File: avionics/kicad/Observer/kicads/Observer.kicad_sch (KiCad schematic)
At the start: 66 parts, among them Q1 AO3400 logic-level N-MOSFET, T1 Wurth 749010012A, T1_CMC1 SRF2012-100Y, T1_CMC2 SRF2012-100Y, T1_D1 PRTR5V0U2X, T1_D2 PRTR5V0U2X, T2 Wurth 749010012A, T2_CMC1 SRF2012-100Y, T2_CMC2 SRF2012-100Y, T2_D1 PRTR5V0U2X, T2_D2 PRTR5V0U2X, U2 Microchip KSZ9477, U3 TI MSPM0G3519-Q1, U4 TI ISOW1044BDFMR, U5 Infineon SLB 9672AU2.0, U6 TI ISOW1412, Y1 25MHz

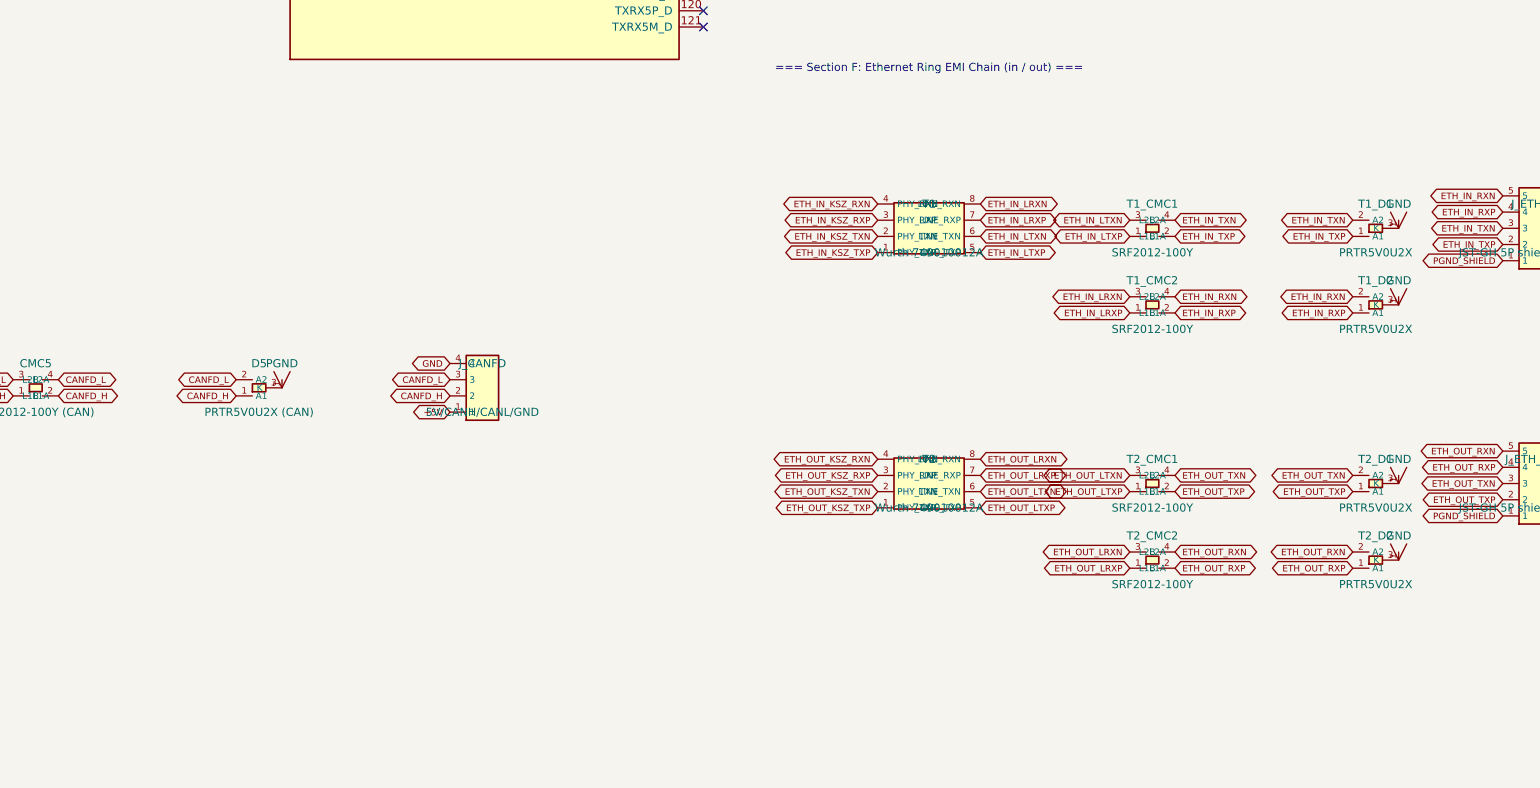
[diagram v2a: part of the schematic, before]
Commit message: fix(avionics): PRTR5V0U2X package/pinout fix on all 12 instances, 5 boards
Owner-approved 2026-09-26 (avionics/WBS.md U7.2). Per Nexperia
PRTR5V0U2X datasheet Table 2 (SOT143B: 1=GND, 2=I/O1, 3=I/O2, 4=VCC),
relinked via tools/kicad_relink.py --rewire (same footprint position/
rotation preserved, only package + pin-to-net correspondence corrected):

- Pilot TVS-CAN, TVS-RS485; TACCO TVS-CAN, TVS-RS485; FlightEngineer
  D_I2C: straightforward SOT-363->SOT-143 swap with existing GND/VCC
  nets carried over unchanged (5 instances).
- Observer T1_D1/T1_D2/T2_D1/T2_D2 (Ethernet magnetics ESD) and D5
  (CAN-FD), Commo 'ANT TVS' and 'UART TVS': these had no VCC net at
  all in the original (wrong-package) design -- VCC tied to the local
  GND/PGND net as a conservative fallback (line-to-line and
  line-to-ground clamping preserved; the rail-clamp direction is
  inert). This is a judgment call, not a datasheet requirement --
  flagged for review, not a silent assumption (7 instances).

ERC unchanged (0/0/0/0/154-pre-existing) on all 5 boards; DRC/parity
flat or improved except one new courtyard-overlap warning on Pilot
(TVS-CAN vs C-IN1, mechanical only) left unresolved rather than guess
a nudge direction without full layout context.

AI-authored: Claude Sonnet 5 (Anthropic).

Co-Authored-By: Claude Sonnet 5 <noreply@anthropic.com>
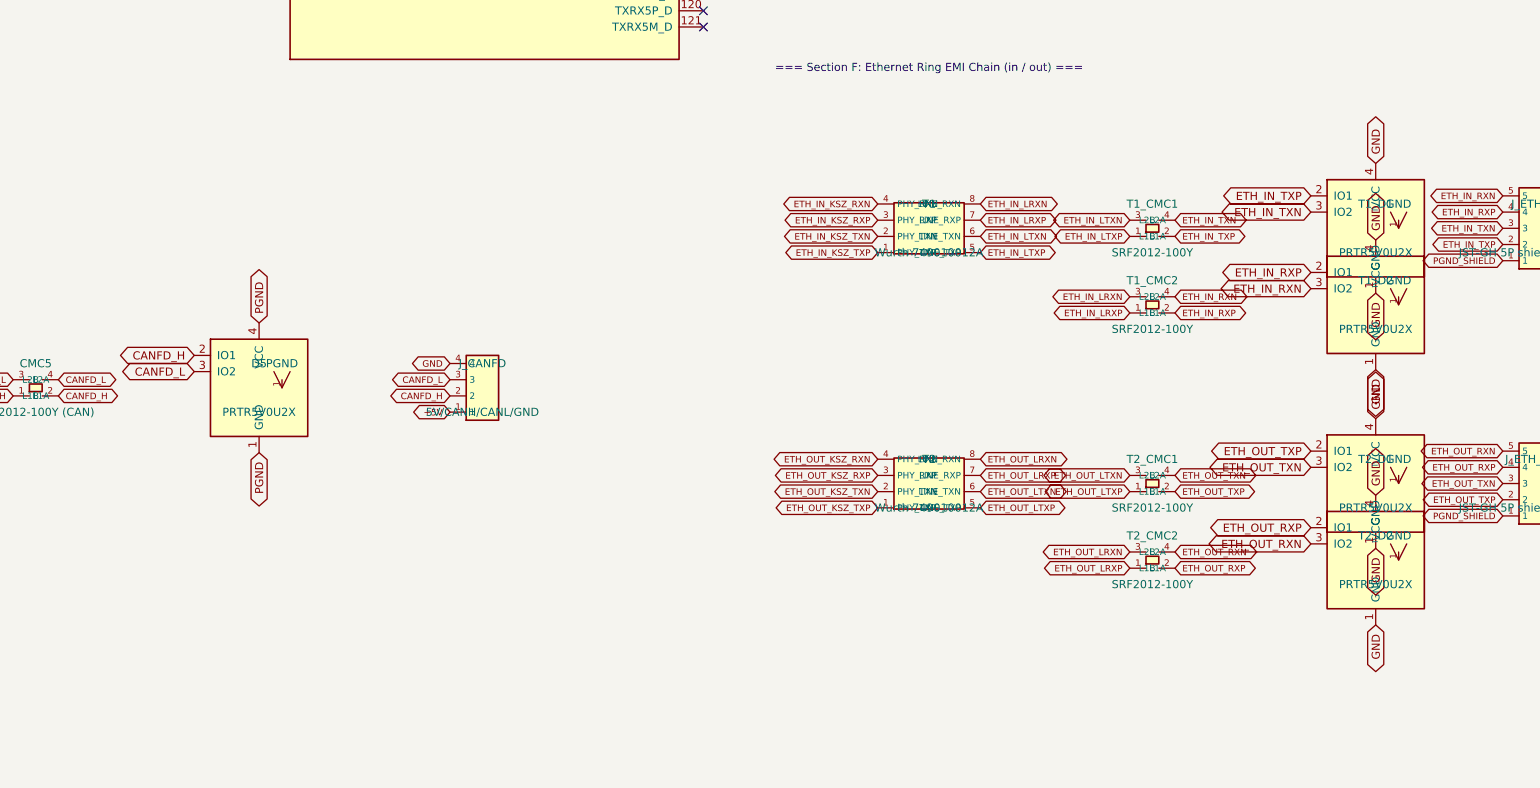
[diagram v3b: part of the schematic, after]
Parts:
- D5: value PRTR5V0U2X (CAN) -> PRTR5V0U2X; footprint Package_TO_SOT_SMD:SOT-363_SC-70-6 -> Package_TO_SOT_SMD:SOT-143; symbol NEXPERIA_PRTR5V0U2X -> SecureControllers:PRTR5V0U2X
- T1_D1, T1_D2, T2_D1, T2_D2: footprint Package_TO_SOT_SMD:SOT-363_SC-70-6 -> Package_TO_SOT_SMD:SOT-143; symbol NEXPERIA_PRTR5V0U2X -> SecureControllers:PRTR5V0U2X
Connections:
- net CANFD_H: now also D5.2 (IO1); no longer D5.1 (A1)
- net CANFD_L: now also D5.3 (IO2); no longer D5.2 (A2)
- net ETH_IN_RXN: now also T1_D2.3 (IO2); no longer T1_D2.2 (A2)
- net ETH_IN_RXP: now also T1_D2.2 (IO1); no longer T1_D2.1 (A1)
- net ETH_IN_TXN: now also T1_D1.3 (IO2); no longer T1_D1.2 (A2)
- net ETH_IN_TXP: now also T1_D1.2 (IO1); no longer T1_D1.1 (A1)
- net ETH_OUT_RXN: now also T2_D2.3 (IO2); no longer T2_D2.2 (A2)
- net ETH_OUT_RXP: now also T2_D2.2 (IO1); no longer T2_D2.1 (A1)
- net ETH_OUT_TXN: now also T2_D1.3 (IO2); no longer T2_D1.2 (A2)
- net ETH_OUT_TXP: now also T2_D1.2 (IO1); no longer T2_D1.1 (A1)
- net GND: now also T1_D1.1 (GND), T1_D1.4 (VCC), T1_D2.1 (GND), T1_D2.4 (VCC), T2_D1.1 (GND), T2_D1.4 (VCC), T2_D2.1 (GND), T2_D2.4 (VCC); no longer T1_D1.3 (K), T1_D2.3 (K), T2_D1.3 (K), T2_D2.3 (K)
- net PGND: now also D5.1 (GND), D5.4 (VCC); no longer D5.3 (K)
